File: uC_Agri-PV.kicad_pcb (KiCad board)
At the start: 4 copper layers, 113 x 113 mm, 248 parts, among them IC1 ESDALC6V1W5, IC2 DMP1045U-7, IC201 ESDALC6V1W5, IC202 ESDALC6V1W5, IC203 ESDALC6V1W5, IC601 MMS9013-L-TP, IC602 MMS9013-L-TP, IC701 TPS63021DSJR, IC8 317990687, J1 PJ-102B, J4 USB_B_Micro, J502 503398-1892, J6 Conn_Coaxial, J601 USB_B_Micro, Q1 IRLML6402, Q2 IRLML6402, Q201 DMG1012T-13, Q202 DMG1012T-13, Q203 DMG1012T-13, Q204 DMG1012T-13, Q501 IRLML6402, Q7 IRLML6402, Q701 IRLML6402, Q8 IRLML6402, Q801 IRLML6402, Q802 IRLML6402, Q803 IRLML6402, Q804 IRLML6402, Q805 IRLML6402, SW1 SW_SPDT, SW2 SW_DIP_x01, SW3 SW_DIP_x01, U201 TLV9304IDR, U202 STM32U575ZIT6Q, U3 ESP32-C6-WROOM-1-N8, U4 AMS1117-3.3, U702 TLV9304IDR, U801 TPS61023DRLR, U802 ISL83078EIBZA, X1 Conn_01x06_Pin, X10 Conn_02x02_Counter_Clockwise, X11 Conn_01x04_Pin, X12 Conn_01x04_Pin, X13 Conn_01x07_Pin, X14 Conn_01x03_Pin, X15 Conn_01x03_Pin, X16 Conn_01x03_Pin, X17 Conn_01x03_Pin, X18 Conn_01x04_Pin, X19 Conn_01x05_Pin, X2 Conn_01x06_Pin, X20 3220-10-0100-00, X21 Conn_01x02_Pin, X22 Conn_01x02_Pin, X3 Conn_01x04_Pin, X4 Conn_01x04_Pin, X5 Conn_01x07_Pin, X6 Conn_01x06_Pin, X601 XTAL_4_PINS, X602 XTAL_2_PINS, X7 Conn_01x04_Pin, X8 Conn_01x04_Pin, X9 Conn_01x04_Pin

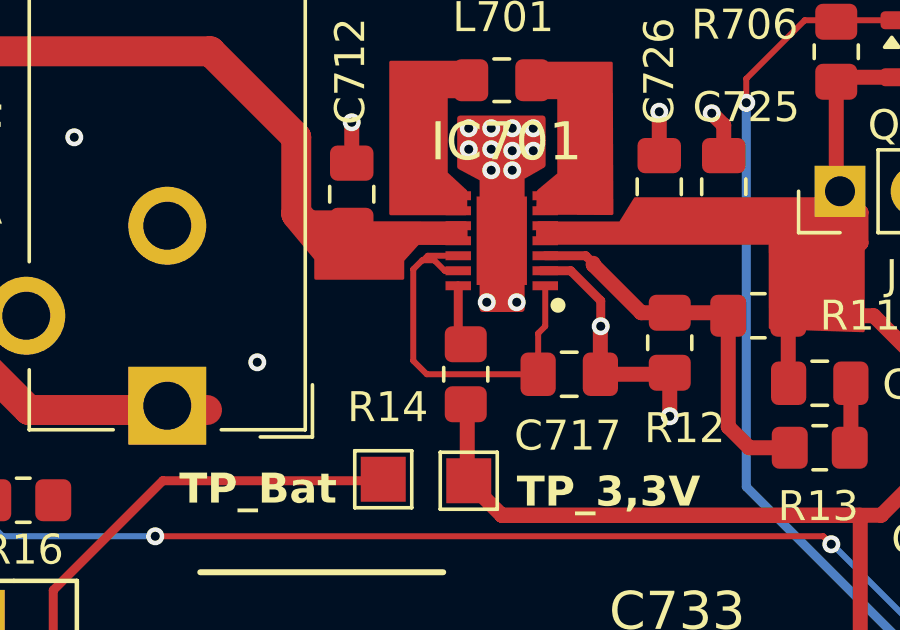
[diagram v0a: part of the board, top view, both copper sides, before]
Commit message: Add board housing STEP files; update KiCad files
Add exported mechanical STEP models for the board housing (CAD/board_housing.step and variants _o, _stg, _u). Also update KiCad project assets and documentation: POWER_CONTROL.md, Power.kicad_sch, STM32.kicad_sch, uC_Agri-PV.kicad_pcb, uC_Agri-PV.kicad_pro, uC_Agri-PV.net, bom/ibom.html and fp-info-cache. These changes synchronize the PCB/schematic/BOM with the new mechanical exports and refresh power/control documentation and footprint cache. Layout is not finished jet.
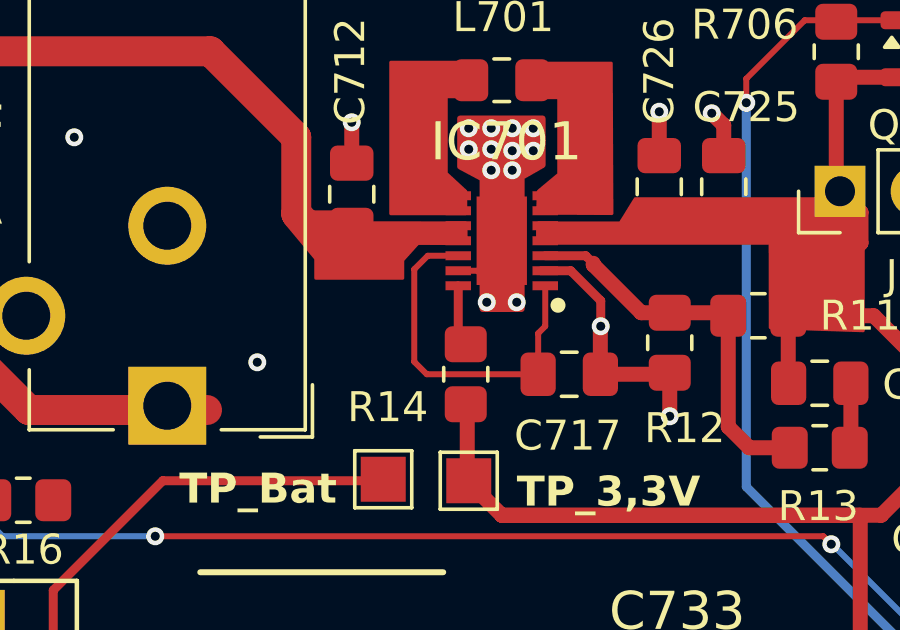
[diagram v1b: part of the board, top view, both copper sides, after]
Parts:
- R11: value 1M -> 0R
- R16: value 1k -> 10k
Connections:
- IC701 pad 13: Net-(IC701-EN) -> GND
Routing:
- net GND: track 162.9 -> 164.7 mm
- net Net-(IC701-EN): track 13.4 -> 12.1 mm
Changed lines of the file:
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@@
 			)
 		)
-		(property "Value" "1M"
+		(property "Value" "0R"
 			(at 0 1.65 0)
 			(layer "F.Fab")
@@
 			)
 		)
-		(property "Value" "1k"
+		(property "Value" "10k"
 			(at 0 1.65 0)
 			(layer "F.Fab")
@@
 		(sheetname "/Power Supply/")
 		(sheetfile "Power.kicad_sch")
-		(attr smd)
+		(attr smd dnp)
 		(fp_line
 			(start -0.227064 -0.735)
@@
 		(sheetname "/Power Supply/")
 		(sheetfile "Power.kicad_sch")
-		(attr smd)
+		(attr smd dnp)
 		(fp_line
 			(start -0.261252 -0.735)
@@
 			(size 0.3 0.85)
 			(layers "F.Cu" "F.Mask" "F.Paste")
-			(net 41 "Net-(IC701-EN)")
+			(net 5 "GND")
 			(pinfunction "PS/SYNC")
 			(pintype "passive")
@@
 	)
 	(segment
+		(start 59.847 45.05)
+		(end 60.15 45.353)
+		(width 0.2)
+		(layer "F.Cu")
+		(net 5)
+	)
+	(segment
 		(start 66.7 137.1)
 		(end 67.3 136.5)
@@
 	)
 	(segment
+		(start 60.15 45.353)
+		(end 60.15 46.1)
+		(width 0.2)
+		(layer "F.Cu")
+		(net 5)
+	)
+	(segment
 		(start 82.3875 44.1)
 		(end 81.33 44.1)
@@
 	)
 	(segment
+		(start 59.2 45.05)
+		(end 59.847 45.05)
+		(width 0.2)
+		(layer "F.Cu")
+		(net 5)
+	)
+	(segment
 		(start 67.7625 89.575)
 		(end 69.225 89.575)
@@
 	)
 	(segment
-		(start 58.75 45.05)
-		(end 59.2 45.05)
-		(width 0.2)
-		(layer "F.Cu")
-		(net 41)
-	)
-	(segment
 		(start 62.1 46.9)
 		(end 62.1 45.55)
@@
 	)
 	(segment
-		(start 57.7 45)
-		(end 58 44.7)
-		(width 0.2)
-		(layer "F.Cu")
-		(net 41)
-	)
-	(segment
-		(start 57.7 48.05)
-		(end 57.7 45)
-		(width 0.2)
-		(layer "F.Cu")
-		(net 41)
-	)
-	(segment
-		(start 58 44.7)
-		(end 58.4 44.7)
+		(start 57.733733 48.083733)
+		(end 57.733733 45)
 		(width 0.2)
 		(layer "F.Cu")
@@
 	(segment
 		(start 58.15 48.5)
-		(end 57.7 48.05)
-		(width 0.2)
-		(layer "F.Cu")
-		(net 41)
-	)
-	(segment
-		(start 58.4 44.7)
-		(end 58.75 45.05)
+		(end 57.733733 48.083733)
 		(width 0.2)
 		(layer "F.Cu")
@@
 	)
 	(segment
-		(start 58.033733 44.7)
+		(start 57.733733 45)
 		(end 58.183733 44.55)
 		(width 0.2)
